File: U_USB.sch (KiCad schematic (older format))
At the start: 15 parts, among them J2 USB_C_Receptacle_USB2.0, U13 ADUM4160

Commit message: begin MCU editing
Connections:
- net USB_FS_N renamed USB_FS_DN
- net USB_FS_P renamed USB_FS_DP
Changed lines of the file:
@@
 $Descr A4 11693 8268
 encoding utf-8
-Sheet 4 10
+Sheet 4 9
 Title ""
 Date ""
@@
 	3240 3850 3650 3850
 Text HLabel 2610 3850 0    50   BiDi ~ 0
-USB_FS_P
+USB_FS_DP
 Text HLabel 2610 3950 0    50   BiDi ~ 0
-USB_FS_N
+USB_FS_DN
 $Comp
 L power:GNDREF #PWR?
@@
 Wire Wire Line
 	3310 3650 3650 3650
+Text Label 2650 3850 0    50   ~ 0
+PA12
+Text Label 2650 3950 0    50   ~ 0
+PA11
 $EndSCHEMATC

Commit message: v0.1
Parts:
- gave numbers to parts that had none: 2
- renumbered C17 to C7, C18 to C8, C19 to C9, J2 to J1, L3 to L1, R21 to R10, R22 to R11, R23 to R12, R24 to R13, R19 to R8, R20 to R9, U13 to U8
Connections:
- no-connect marks 2 -> 4
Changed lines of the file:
@@
 $Descr A4 11693 8268
 encoding utf-8
-Sheet 4 9
-Title ""
-Date ""
-Rev ""
-Comp ""
-Comment1 ""
+Sheet 3 9
+Title "ШВУ"
+Date "2021-03-25"
+Rev "V0.1"
+Comp "ЦВЕТМЕТНАЛАДКА"
+Comment1 "Шустов В.И."
 Comment2 ""
 Comment3 ""
@@
 $EndComp
 $Comp
-L Connector:USB_C_Receptacle_USB2.0 J2
+L Connector:USB_C_Receptacle_USB2.0 J1
 U 1 1 609A5203
 P 7090 3740
-F 0 "J2" H 7160 4600 50  0000 R CNN
+F 0 "J1" H 7160 4600 50  0000 R CNN
 F 1 "USB_C_Receptacle_USB2.0" H 7590 4510 50  0000 R CNN
 F 2 "Connector_USB:USB_C_Receptacle_Palconn_UTC16-G" H 7240 3740 50  0001 C CNN
@@
 	5730 5350 5730 5460
 $Comp
-L Interface_USB:ADUM4160 U13
+L Interface_USB:ADUM4160 U8
 U 1 1 60CF7C1F
 P 4150 3950
-F 0 "U13" H 3780 4610 50  0000 C CNN
+F 0 "U8" H 3780 4610 50  0000 C CNN
 F 1 "ADUM4160" H 3780 4520 50  0000 C CNN
 F 2 "Package_SO:SOIC-16W_7.5x10.3mm_P1.27mm" H 4150 3250 50  0001 C CNN
@@
 P 6130 5040
 AR Path="/608C7842/60CFFF64" Ref="R?"  Part="1"
-AR Path="/6099558B/60CFFF64" Ref="R23"  Part="1"
-F 0 "R23" H 6190 5090 50  0000 L CNN
+AR Path="/6099558B/60CFFF64" Ref="R12"  Part="1"
+F 0 "R12" H 6190 5090 50  0000 L CNN
 F 1 "5,1K" H 6190 5000 50  0000 L CNN
 F 2 "Resistor_SMD:R_0805_2012Metric_Pad1.20x1.40mm_HandSolder" V 6060 5040 50  0001 C CNN
@@
 P 6420 5040
 AR Path="/608C7842/60D0043D" Ref="R?"  Part="1"
-AR Path="/6099558B/60D0043D" Ref="R24"  Part="1"
-F 0 "R24" H 6480 5090 50  0000 L CNN
+AR Path="/6099558B/60D0043D" Ref="R13"  Part="1"
+F 0 "R13" H 6480 5090 50  0000 L CNN
 F 1 "5,1K" H 6480 5000 50  0000 L CNN
 F 2 "Resistor_SMD:R_0805_2012Metric_Pad1.20x1.40mm_HandSolder" V 6350 5040 50  0001 C CNN
@@
 P 4930 3850
 AR Path="/608C7842/60D017E8" Ref="R?"  Part="1"
-AR Path="/6099558B/60D017E8" Ref="R20"  Part="1"
-F 0 "R20" V 4770 3800 50  0000 L CNN
+AR Path="/6099558B/60D017E8" Ref="R9"  Part="1"
+F 0 "R9" V 4770 3800 50  0000 L CNN
 F 1 "24" V 4840 3800 50  0000 L CNN
 F 2 "Resistor_SMD:R_0805_2012Metric_Pad1.20x1.40mm_HandSolder" V 4860 3850 50  0001 C CNN
@@
 P 4930 3950
 AR Path="/608C7842/60D02204" Ref="R?"  Part="1"
-AR Path="/6099558B/60D02204" Ref="R22"  Part="1"
-F 0 "R22" V 5020 3900 50  0000 L CNN
+AR Path="/6099558B/60D02204" Ref="R11"  Part="1"
+F 0 "R11" V 5020 3900 50  0000 L CNN
 F 1 "24" V 5090 3900 50  0000 L CNN
 F 2 "Resistor_SMD:R_0805_2012Metric_Pad1.20x1.40mm_HandSolder" V 4860 3950 50  0001 C CNN
@@
 P 5150 4880
 AR Path="/60D39D51" Ref="C?"  Part="1"
-AR Path="/6099558B/60D39D51" Ref="C19"  Part="1"
-F 0 "C19" H 4870 4910 50  0000 L CNN
+AR Path="/6099558B/60D39D51" Ref="C9"  Part="1"
+F 0 "C9" H 4870 4910 50  0000 L CNN
 F 1 "1µF" H 4870 4830 50  0000 L CNN
 F 2 "Capacitor_SMD:C_0603_1608Metric_Pad1.08x0.95mm_HandSolder" H 5188 4730 50  0001 C CNN
@@
 P 4720 4880
 AR Path="/60D3AA9C" Ref="C?"  Part="1"
-AR Path="/6099558B/60D3AA9C" Ref="C18"  Part="1"
-F 0 "C18" H 4440 4910 50  0000 L CNN
+AR Path="/6099558B/60D3AA9C" Ref="C8"  Part="1"
+F 0 "C8" H 4440 4910 50  0000 L CNN
 F 1 "1µF" H 4440 4830 50  0000 L CNN
 F 2 "Capacitor_SMD:C_0603_1608Metric_Pad1.08x0.95mm_HandSolder" H 4758 4730 50  0001 C CNN
@@
 P 3560 4880
 AR Path="/60D3F7A8" Ref="C?"  Part="1"
-AR Path="/6099558B/60D3F7A8" Ref="C17"  Part="1"
-F 0 "C17" H 3675 4926 50  0000 L CNN
+AR Path="/6099558B/60D3F7A8" Ref="C7"  Part="1"
+F 0 "C7" H 3675 4926 50  0000 L CNN
 F 1 "1µF" H 3675 4835 50  0000 L CNN
 F 2 "Capacitor_SMD:C_0603_1608Metric_Pad1.08x0.95mm_HandSolder" H 3598 4730 50  0001 C CNN
@@
 AR Path="/60D4C56E" Ref="#PWR?"  Part="1"
 AR Path="/60A03F8A/60D4C56E" Ref="#PWR?"  Part="1"
-AR Path="/6099558B/60D4C56E" Ref="#PWR013"  Part="1"
-F 0 "#PWR013" H 3740 5300 50  0001 C CNN
+AR Path="/6099558B/60D4C56E" Ref="#PWR010"  Part="1"
+F 0 "#PWR010" H 3740 5300 50  0001 C CNN
 F 1 "GNDREF" H 3745 5377 50  0001 C CNN
 F 2 "" H 3740 5550 50  0001 C CNN
@@
 	3740 3140 4050 3140
 $Comp
-L SVIELCOM_Library:VDD_PER #PWR012
+L SVIELCOM_Library:VDD_PER #PWR09
 U 1 1 60D5551E
 P 3740 2710
-F 0 "#PWR012" H 3740 2560 50  0001 C CNN
+F 0 "#PWR09" H 3740 2560 50  0001 C CNN
 F 1 "VDD_PER" H 3760 2883 50  0000 C CNN
 F 2 "" H 3740 2710 50  0001 C CNN
@@
 AR Path="/60A03F8A/60D586A1" Ref="L?"  Part="1"
 AR Path="/608C7842/60D586A1" Ref="L?"  Part="1"
-AR Path="/6099558B/60D586A1" Ref="L3"  Part="1"
-F 0 "L3" H 3792 2906 50  0000 L CNN
+AR Path="/6099558B/60D586A1" Ref="L1"  Part="1"
+F 0 "L1" H 3792 2906 50  0000 L CNN
 F 1 "600R@100MHz" H 3792 2815 50  0000 L CNN
 F 2 "" H 3740 2860 50  0001 C CNN
@@
 P 3090 3850
 AR Path="/608C7842/60D5DE57" Ref="R?"  Part="1"
-AR Path="/6099558B/60D5DE57" Ref="R19"  Part="1"
-F 0 "R19" V 2930 3800 50  0000 L CNN
+AR Path="/6099558B/60D5DE57" Ref="R8"  Part="1"
+F 0 "R8" V 2930 3800 50  0000 L CNN
 F 1 "24" V 3000 3800 50  0000 L CNN
 F 2 "Resistor_SMD:R_0805_2012Metric_Pad1.20x1.40mm_HandSolder" V 3020 3850 50  0001 C CNN
@@
 P 3090 3950
 AR Path="/608C7842/60D5DE5D" Ref="R?"  Part="1"
-AR Path="/6099558B/60D5DE5D" Ref="R21"  Part="1"
-F 0 "R21" V 3180 3900 50  0000 L CNN
+AR Path="/6099558B/60D5DE5D" Ref="R10"  Part="1"
+F 0 "R10" V 3180 3900 50  0000 L CNN
 F 1 "24" V 3250 3900 50  0000 L CNN
 F 2 "Resistor_SMD:R_0805_2012Metric_Pad1.20x1.40mm_HandSolder" V 3020 3950 50  0001 C CNN
@@
 Connection ~ 5830 3950
 Wire Wire Line
-	4720 5460 5150 5460
+	4720 5460 4920 5460
 Wire Wire Line
 	5150 5030 5150 5460
@@
 Connection ~ 5150 3140
 Wire Wire Line
-	5150 3140 6490 3140
+	5150 3140 5440 3140
 $Comp
 L Device:CP C?
@@
 P 3150 4880
 AR Path="/60D855B5" Ref="C?"  Part="1"
-AR Path="/6099558B/60D855B5" Ref="C?"  Part="1"
-F 0 "C?" H 3268 4926 50  0000 L CNN
+AR Path="/6099558B/60D855B5" Ref="C6"  Part="1"
+F 0 "C6" H 3268 4926 50  0000 L CNN
 F 1 "10µF" H 3268 4835 50  0000 L CNN
 F 2 "Capacitor_Tantalum_SMD:CP_EIA-3216-10_Kemet-I" H 3188 4730 50  0001 C CNN
@@
 P 3310 3380
 AR Path="/608C7842/60926224" Ref="R?"  Part="1"
-AR Path="/6099558B/60926224" Ref="R?"  Part="1"
-F 0 "R?" H 3150 3370 50  0000 L CNN
+AR Path="/6099558B/60926224" Ref="R7"  Part="1"
+F 0 "R7" H 3150 3370 50  0000 L CNN
 F 1 "10K" H 3100 3450 50  0000 L CNN
 F 2 "Resistor_SMD:R_0805_2012Metric_Pad1.20x1.40mm_HandSolder" V 3240 3380 50  0001 C CNN
@@
 Text Label 2650 3950 0    50   ~ 0
 PA11
+NoConn ~ 5930 4750
+NoConn ~ 5530 4750
+$Comp
+L power:PWR_FLAG #FLG02
+U 1 1 610C9C05
+P 5440 3140
+F 0 "#FLG02" H 5440 3215 50  0001 C CNN
+F 1 "PWR_FLAG" H 5440 3313 50  0001 C CNN
+F 2 "" H 5440 3140 50  0001 C CNN
+F 3 "~" H 5440 3140 50  0001 C CNN
+	1    5440 3140
+	1    0    0    -1
+$EndComp
+Connection ~ 5440 3140
+Wire Wire Line
+	5440 3140 6490 3140
+$Comp
+L power:PWR_FLAG #FLG03
+U 1 1 610CA697
+P 4920 5460
+F 0 "#FLG03" H 4920 5535 50  0001 C CNN
+F 1 "PWR_FLAG" H 4920 5633 50  0001 C CNN
+F 2 "" H 4920 5460 50  0001 C CNN
+F 3 "~" H 4920 5460 50  0001 C CNN
+	1    4920 5460
+	1    0    0    -1
+$EndComp
+Connection ~ 4920 5460
+Wire Wire Line
+	4920 5460 5150 5460
+$Comp
+L power:PWR_FLAG #FLG01
+U 1 1 6111B634
+P 3560 3140
+F 0 "#FLG01" H 3560 3215 50  0001 C CNN
+F 1 "PWR_FLAG" H 3580 3340 50  0001 C CNN
+F 2 "" H 3560 3140 50  0001 C CNN
+F 3 "~" H 3560 3140 50  0001 C CNN
+	1    3560 3140
+	1    0    0    -1
+$EndComp
 $EndSCHEMATC

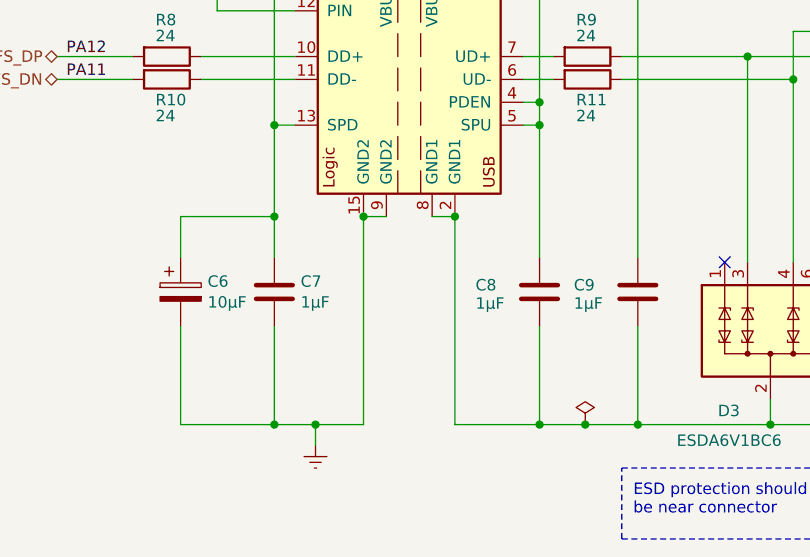
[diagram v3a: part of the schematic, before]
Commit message: v0.3 changed sd_card holder
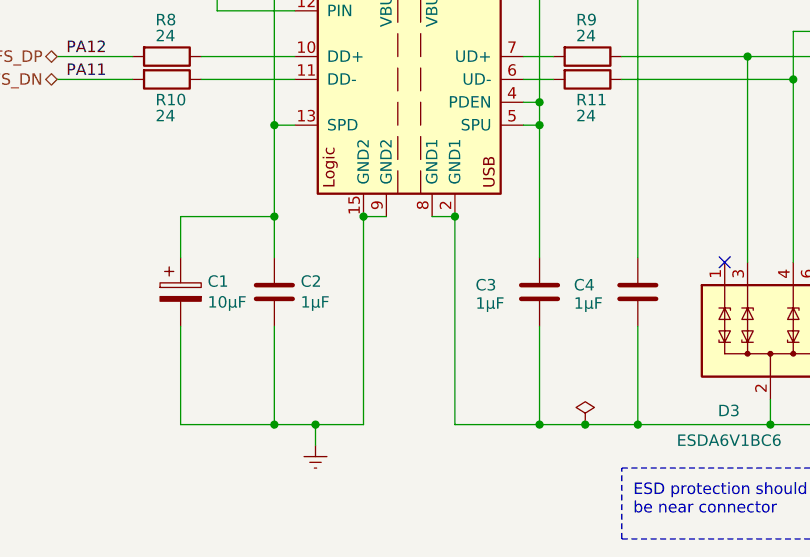
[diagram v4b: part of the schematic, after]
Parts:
- renumbered C6 to C1, C7 to C2, C8 to C3, C9 to C4
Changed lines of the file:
@@
 P 5150 4880
 AR Path="/60D39D51" Ref="C?"  Part="1"
-AR Path="/6099558B/60D39D51" Ref="C9"  Part="1"
-F 0 "C9" H 4870 4910 50  0000 L CNN
+AR Path="/6099558B/60D39D51" Ref="C4"  Part="1"
+F 0 "C4" H 4870 4910 50  0000 L CNN
 F 1 "1µF" H 4870 4830 50  0000 L CNN
 F 2 "Capacitor_SMD:C_0603_1608Metric_Pad1.08x0.95mm_HandSolder" H 5188 4730 50  0001 C CNN
@@
 P 4720 4880
 AR Path="/60D3AA9C" Ref="C?"  Part="1"
-AR Path="/6099558B/60D3AA9C" Ref="C8"  Part="1"
-F 0 "C8" H 4440 4910 50  0000 L CNN
+AR Path="/6099558B/60D3AA9C" Ref="C3"  Part="1"
+F 0 "C3" H 4440 4910 50  0000 L CNN
 F 1 "1µF" H 4440 4830 50  0000 L CNN
 F 2 "Capacitor_SMD:C_0603_1608Metric_Pad1.08x0.95mm_HandSolder" H 4758 4730 50  0001 C CNN
@@
 P 3560 4880
 AR Path="/60D3F7A8" Ref="C?"  Part="1"
-AR Path="/6099558B/60D3F7A8" Ref="C7"  Part="1"
-F 0 "C7" H 3675 4926 50  0000 L CNN
+AR Path="/6099558B/60D3F7A8" Ref="C2"  Part="1"
+F 0 "C2" H 3675 4926 50  0000 L CNN
 F 1 "1µF" H 3675 4835 50  0000 L CNN
 F 2 "Capacitor_SMD:C_0603_1608Metric_Pad1.08x0.95mm_HandSolder" H 3598 4730 50  0001 C CNN
@@
 P 3150 4880
 AR Path="/60D855B5" Ref="C?"  Part="1"
-AR Path="/6099558B/60D855B5" Ref="C6"  Part="1"
-F 0 "C6" H 3268 4926 50  0000 L CNN
+AR Path="/6099558B/60D855B5" Ref="C1"  Part="1"
+F 0 "C1" H 3268 4926 50  0000 L CNN
 F 1 "10µF" H 3268 4835 50  0000 L CNN
 F 2 "Capacitor_Tantalum_SMD:CP_EIA-3216-10_Kemet-I" H 3188 4730 50  0001 C CNN

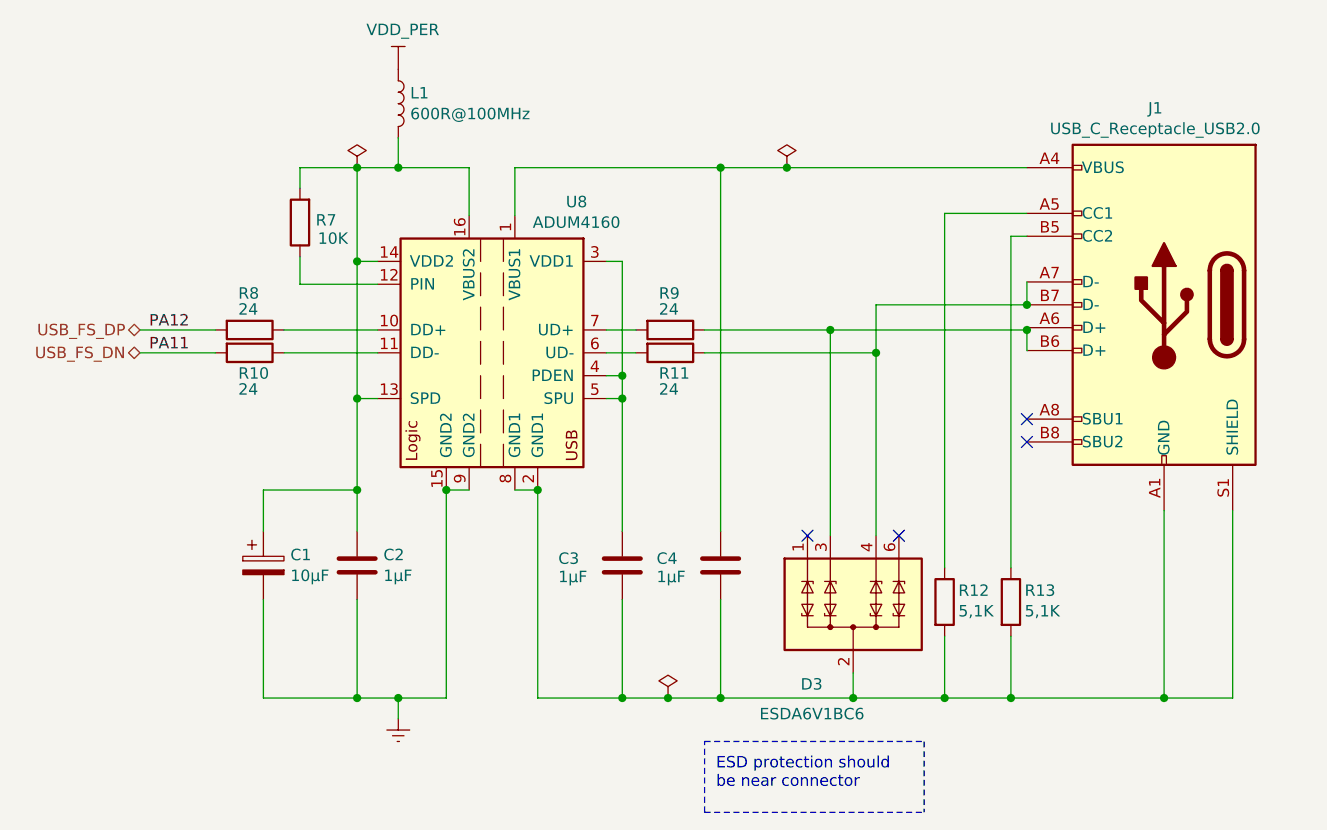
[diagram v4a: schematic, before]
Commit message: footprints associations is done
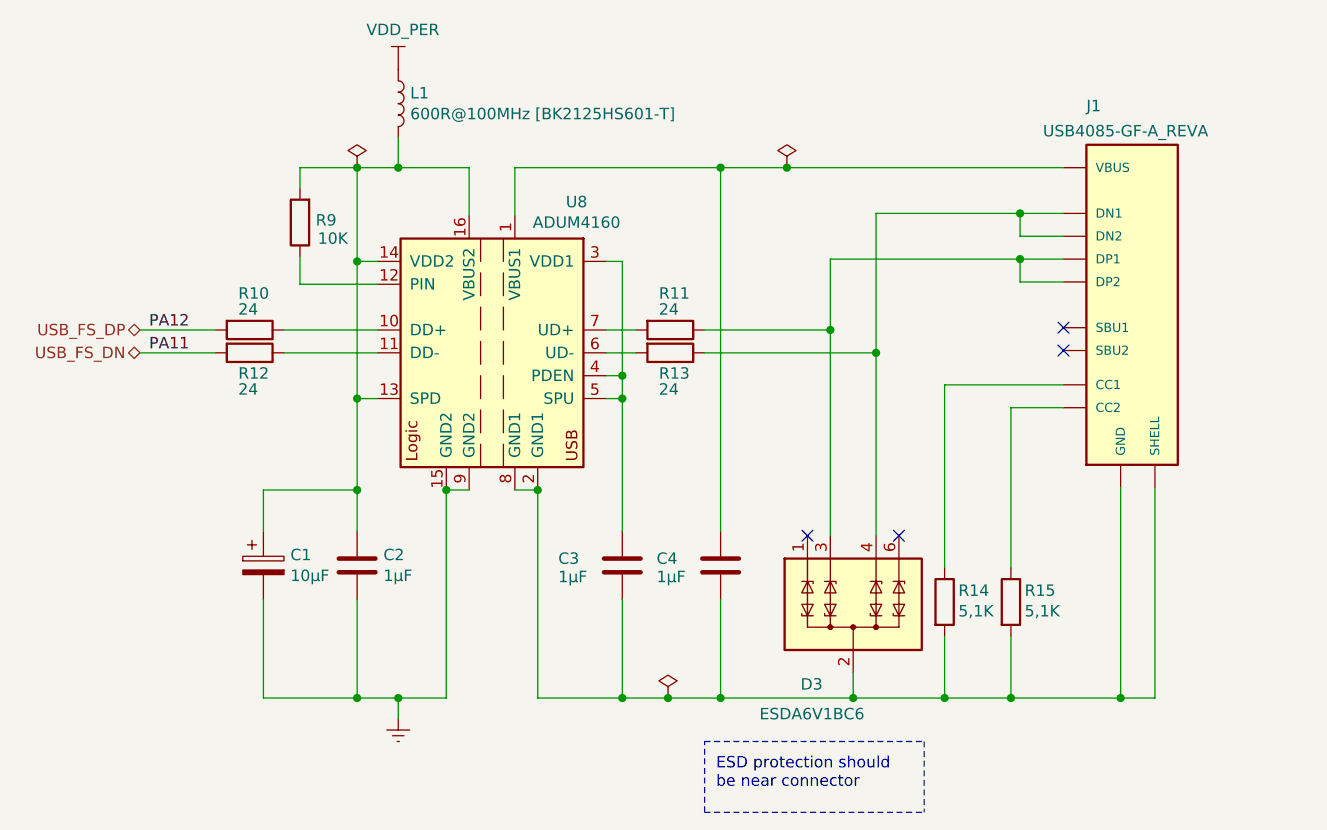
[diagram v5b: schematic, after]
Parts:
- removed J1: USB_C_Receptacle_USB2.0, Connector_USB:USB_C_Receptacle_Palconn_UTC16-G, symbol Connector:USB_C_Receptacle_USB2.0
- added J1: USB4085-GF-A_REVA, SVIELCOM:GCT_USB4085-GF-A_REVA, symbol SVIELCOM_Library:USB4085-GF-A_REVA
- L1: value 600R@100MHz -> 600R@100MHz [BK2125HS601-T]; footprint (none) -> Inductor_SMD:L_0805_2012Metric_Pad1.15x1.40mm_HandSolder
- renumbered R8 to R10, R9 to R11, R10 to R12, R11 to R13, R12 to R14, R13 to R15, R7 to R9
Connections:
- net at C3.2, C4.2, D3.2 (COM)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: now also J1.A1 (GND), J1.A12 (GND), J1.B1 (GND), J1.B12 (GND), J1.P1 (SHELL), J1.P2 (SHELL), J1.P3 (SHELL), J1.P4 (SHELL)
- net at D3.3 (TVS2), R11.1: now also J1.A6 (DP1), J1.B6 (DP2)
- net at D3.4 (TVS3), R13.1: now also J1.A7 (DN1), J1.B7 (DN2)
- net at C4.1, U8.1 (VBUS1): now also J1.A4 (VBUS), J1.A9 (VBUS), J1.B4 (VBUS), J1.B9 (VBUS)
- net at R14.1: now also J1.A5 (CC1)
- net at R15.1: now also J1.B5 (CC2)
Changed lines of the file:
@@
 Title "ШВУ"
 Date "2021-03-25"
-Rev "V0.1"
+Rev "V0.3"
 Comp "ЦВЕТМЕТНАЛАДКА"
 Comment1 "Шустов В.И."
@@
 	1    0    0    -1
 $EndComp
-$Comp
-L Connector:USB_C_Receptacle_USB2.0 J1
-U 1 1 609A5203
-P 7090 3740
-F 0 "J1" H 7160 4600 50  0000 R CNN
-F 1 "USB_C_Receptacle_USB2.0" H 7590 4510 50  0000 R CNN
-F 2 "Connector_USB:USB_C_Receptacle_Palconn_UTC16-G" H 7240 3740 50  0001 C CNN
-F 3 "https://www.usb.org/sites/default/files/documents/usb_type-c.zip" H 7240 3740 50  0001 C CNN
-	1    7090 3740
-	-1   0    0    -1
-$EndComp
-Wire Wire Line
-	6490 3840 6490 3850
-Wire Wire Line
-	6490 3640 6490 3740
 Wire Wire Line
 	5630 4750 5630 3850
@@
 P 6130 5040
 AR Path="/608C7842/60CFFF64" Ref="R?"  Part="1"
-AR Path="/6099558B/60CFFF64" Ref="R12"  Part="1"
-F 0 "R12" H 6190 5090 50  0000 L CNN
+AR Path="/6099558B/60CFFF64" Ref="R14"  Part="1"
+F 0 "R14" H 6190 5090 50  0000 L CNN
 F 1 "5,1K" H 6190 5000 50  0000 L CNN
 F 2 "Resistor_SMD:R_0805_2012Metric_Pad1.20x1.40mm_HandSolder" V 6060 5040 50  0001 C CNN
@@
 P 6420 5040
 AR Path="/608C7842/60D0043D" Ref="R?"  Part="1"
-AR Path="/6099558B/60D0043D" Ref="R13"  Part="1"
-F 0 "R13" H 6480 5090 50  0000 L CNN
+AR Path="/6099558B/60D0043D" Ref="R15"  Part="1"
+F 0 "R15" H 6480 5090 50  0000 L CNN
 F 1 "5,1K" H 6480 5000 50  0000 L CNN
 F 2 "Resistor_SMD:R_0805_2012Metric_Pad1.20x1.40mm_HandSolder" V 6350 5040 50  0001 C CNN
@@
 P 4930 3850
 AR Path="/608C7842/60D017E8" Ref="R?"  Part="1"
-AR Path="/6099558B/60D017E8" Ref="R9"  Part="1"
-F 0 "R9" V 4770 3800 50  0000 L CNN
+AR Path="/6099558B/60D017E8" Ref="R11"  Part="1"
+F 0 "R11" V 4770 3800 50  0000 L CNN
 F 1 "24" V 4840 3800 50  0000 L CNN
 F 2 "Resistor_SMD:R_0805_2012Metric_Pad1.20x1.40mm_HandSolder" V 4860 3850 50  0001 C CNN
@@
 P 4930 3950
 AR Path="/608C7842/60D02204" Ref="R?"  Part="1"
-AR Path="/6099558B/60D02204" Ref="R11"  Part="1"
-F 0 "R11" V 5020 3900 50  0000 L CNN
+AR Path="/6099558B/60D02204" Ref="R13"  Part="1"
+F 0 "R13" V 5020 3900 50  0000 L CNN
 F 1 "24" V 5090 3900 50  0000 L CNN
 F 2 "Resistor_SMD:R_0805_2012Metric_Pad1.20x1.40mm_HandSolder" V 4860 3950 50  0001 C CNN
@@
 	6130 5190 6130 5460
 Wire Wire Line
-	6490 3340 6130 3340
-Wire Wire Line
-	6420 3440 6490 3440
-Wire Wire Line
-	6420 3440 6420 4890
-Wire Wire Line
-	6130 3340 6130 4890
-Connection ~ 6490 3850
-Wire Wire Line
-	6490 3850 6490 3940
-Wire Wire Line
-	5830 3950 5830 3740
-Wire Wire Line
-	5830 3740 6490 3740
-Connection ~ 6490 3740
-NoConn ~ 6490 4240
-NoConn ~ 6490 4340
-Wire Wire Line
-	7090 5460 7090 4640
-Wire Wire Line
-	7390 4640 7390 5460
-Wire Wire Line
-	7390 5460 7090 5460
-Connection ~ 7090 5460
+	6650 4090 6130 4090
+Wire Wire Line
+	6420 4190 6650 4190
+Wire Wire Line
+	6420 4190 6420 4890
+Wire Wire Line
+	6130 4090 6130 4890
+Wire Wire Line
+	6900 5460 6900 4540
+Wire Wire Line
+	7050 4540 7050 5460
+Wire Wire Line
+	7050 5460 6900 5460
+Connection ~ 6900 5460
 Wire Wire Line
 	4650 3550 4720 3550
@@
 AR Path="/6099558B/60D586A1" Ref="L1"  Part="1"
 F 0 "L1" H 3792 2906 50  0000 L CNN
-F 1 "600R@100MHz" H 3792 2815 50  0000 L CNN
-F 2 "" H 3740 2860 50  0001 C CNN
-F 3 "~" H 3740 2860 50  0001 C CNN
+F 1 "600R@100MHz [BK2125HS601-T]" H 3792 2815 50  0000 L CNN
+F 2 "Inductor_SMD:L_0805_2012Metric_Pad1.15x1.40mm_HandSolder" H 3740 2860 50  0001 C CNN
+F 3 "https://www.terraelectronica.ru/pdf/show?pdf_file=http%253A%252F%252Fwww.mouser.com%252Fds%252F2%252F396%252Fmlci07_e-9531.pdf" H 3740 2860 50  0001 C CNN
 	1    3740 2860
 	1    0    0    -1
@@
 P 3090 3850
 AR Path="/608C7842/60D5DE57" Ref="R?"  Part="1"
-AR Path="/6099558B/60D5DE57" Ref="R8"  Part="1"
-F 0 "R8" V 2930 3800 50  0000 L CNN
+AR Path="/6099558B/60D5DE57" Ref="R10"  Part="1"
+F 0 "R10" V 2930 3800 50  0000 L CNN
 F 1 "24" V 3000 3800 50  0000 L CNN
 F 2 "Resistor_SMD:R_0805_2012Metric_Pad1.20x1.40mm_HandSolder" V 3020 3850 50  0001 C CNN
@@
 P 3090 3950
 AR Path="/608C7842/60D5DE5D" Ref="R?"  Part="1"
-AR Path="/6099558B/60D5DE5D" Ref="R10"  Part="1"
-F 0 "R10" V 3180 3900 50  0000 L CNN
+AR Path="/6099558B/60D5DE5D" Ref="R12"  Part="1"
+F 0 "R12" V 3180 3900 50  0000 L CNN
 F 1 "24" V 3250 3900 50  0000 L CNN
 F 2 "Resistor_SMD:R_0805_2012Metric_Pad1.20x1.40mm_HandSolder" V 3020 3950 50  0001 C CNN
@@
 Connection ~ 6420 5460
 Wire Wire Line
-	6420 5460 7090 5460
+	6420 5460 6900 5460
 Connection ~ 6130 5460
 Wire Wire Line
 	6130 5460 6420 5460
-Connection ~ 5630 3850
-Wire Wire Line
-	5630 3850 6490 3850
 Connection ~ 5730 5460
 Wire Wire Line
@@
 P 3310 3380
 AR Path="/608C7842/60926224" Ref="R?"  Part="1"
-AR Path="/6099558B/60926224" Ref="R7"  Part="1"
-F 0 "R7" H 3150 3370 50  0000 L CNN
+AR Path="/6099558B/60926224" Ref="R9"  Part="1"
+F 0 "R9" H 3150 3370 50  0000 L CNN
 F 1 "10K" H 3100 3450 50  0000 L CNN
 F 2 "Resistor_SMD:R_0805_2012Metric_Pad1.20x1.40mm_HandSolder" V 3240 3380 50  0001 C CNN
@@
 Connection ~ 5440 3140
 Wire Wire Line
-	5440 3140 6490 3140
+	5440 3140 6650 3140
 $Comp
 L power:PWR_FLAG #FLG03
@@
 	1    0    0    -1
 $EndComp
+$Comp
+L SVIELCOM_Library:USB4085-GF-A_REVA J1
+U 1 1 617291D1
+P 6950 3740
+F 0 "J1" H 6750 4610 50  0000 L CNN
+F 1 "USB4085-GF-A_REVA" H 6560 4500 50  0000 L CNN
+F 2 "SVIELCOM:GCT_USB4085-GF-A_REVA" H 7200 4390 50  0001 L BNN
+F 3 "https://www.farnell.com/cad/2648880.pdf" H 6950 3740 50  0001 L BNN
+F 4 "A2" H 7200 4490 50  0001 L BNN "PARTREV"
+F 5 "3.46mm" H 7200 4040 50  0001 L BNN "MAXIMUM_PACKAGE_HEIGHT"
+F 6 "Manufacturer Recommendations" H 7200 4290 50  0001 L BNN "STANDARD"
+F 7 "Global Connector Technology" H 7200 4190 50  0001 L BNN "MANUFACTURER"
+	1    6950 3740
+	1    0    0    -1
+$EndComp
+Wire Wire Line
+	6650 3340 6460 3340
+Wire Wire Line
+	6650 3540 6460 3540
+Wire Wire Line
+	5630 3540 5630 3850
+Connection ~ 5630 3850
+Wire Wire Line
+	6650 3640 6460 3640
+Wire Wire Line
+	6460 3640 6460 3540
+Connection ~ 6460 3540
+Wire Wire Line
+	6460 3540 5630 3540
+Wire Wire Line
+	5830 3340 5830 3950
+Wire Wire Line
+	6650 3440 6460 3440
+Wire Wire Line
+	6460 3440 6460 3340
+Connection ~ 6460 3340
+Wire Wire Line
+	6460 3340 5830 3340
+NoConn ~ 6650 3840
+NoConn ~ 6650 3940
 $EndSCHEMATC
